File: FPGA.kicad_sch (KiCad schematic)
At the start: 15 parts, among them U3 XC7A100T-FTG256, U5 S25FL127S

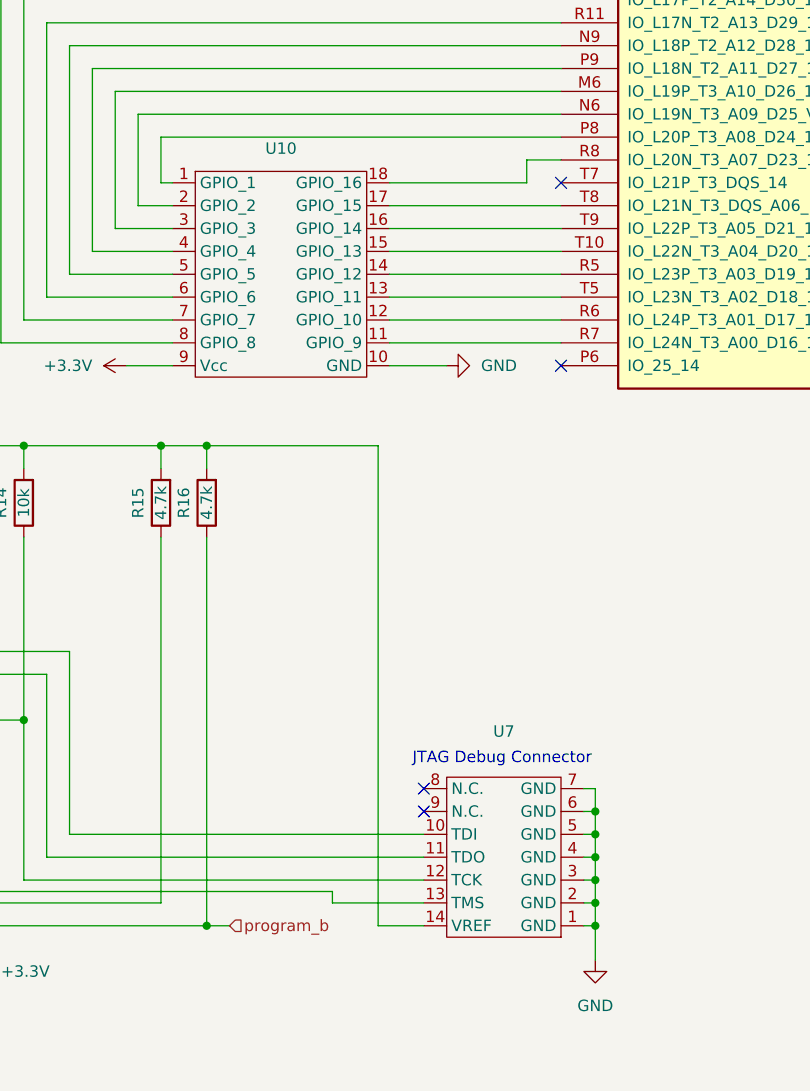
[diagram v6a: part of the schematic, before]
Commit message: Corrected FPGA Debug pin order
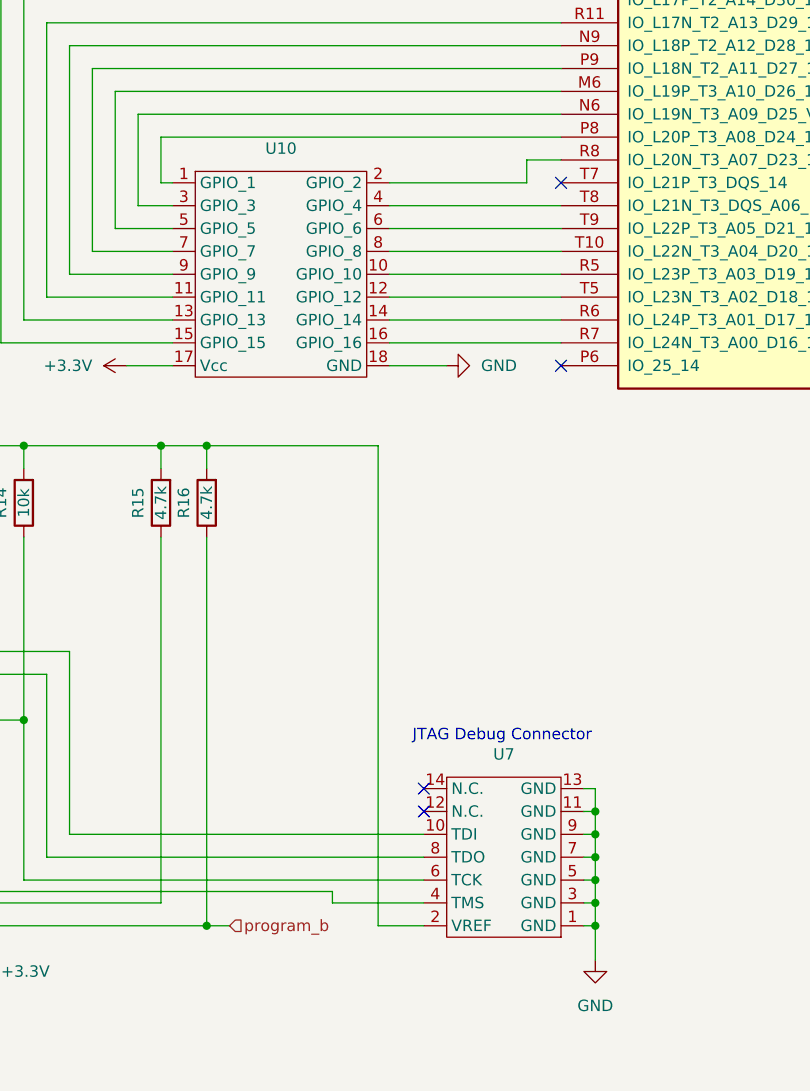
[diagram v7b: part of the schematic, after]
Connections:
- net +3.3V: now also U10.17 (Vcc), U7.2 (VREF); no longer U10.9 (Vcc), U7.14 (VREF)
- net GND: now also U10.18 (GND), U7.11 (GND), U7.13 (GND), U7.9 (GND); no longer U10.10 (GND), U7.2 (GND), U7.4 (GND), U7.6 (GND)
- net at R14.1, U3.L7 (TCK_0): now also U7.6 (TCK); no longer U7.12 (TCK)
- net at U3.M6 (IO_L19P_T3_A10_D26_14): now also U10.5 (GPIO_5); no longer U10.3 (GPIO_3)
- net at U3.N6 (IO_L19N_T3_A09_D25_VREF_14): now also U10.3 (GPIO_3); no longer U10.2 (GPIO_2)
- net at U3.N9 (IO_L18P_T2_A12_D28_14): now also U10.9 (GPIO_9); no longer U10.5 (GPIO_5)
- net at U3.P9 (IO_L18N_T2_A11_D27_14): now also U10.7 (GPIO_7); no longer U10.4 (GPIO_4)
- net at U3.R10 (IO_L17P_T2_A14_D30_14): now also U10.13 (GPIO_13); no longer U10.7 (GPIO_7)
- net at U3.R11 (IO_L17N_T2_A13_D29_14): now also U10.11 (GPIO_11); no longer U10.6 (GPIO_6)
- net at U3.R5 (IO_L23P_T3_A03_D19_14): now also U10.10 (GPIO_10); no longer U10.14 (GPIO_12)
- net at U3.R6 (IO_L24P_T3_A01_D17_14): now also U10.14 (GPIO_14); no longer U10.12 (GPIO_10)
- net at U3.R7 (IO_L24N_T3_A00_D16_14): now also U10.16 (GPIO_16); no longer U10.11 (GPIO_9)
- net at U3.R8 (IO_L20N_T3_A07_D23_14): now also U10.2 (GPIO_2); no longer U10.18 (GPIO_16)
- net at U3.T10 (IO_L22N_T3_A04_D20_14): now also U10.8 (GPIO_8); no longer U10.15 (GPIO_13)
- net at U3.T13 (IO_L16N_T2_A15_D31_14): now also U10.15 (GPIO_15); no longer U10.8 (GPIO_8)
- net at U3.T5 (IO_L23N_T3_A02_D18_14): now also U10.12 (GPIO_12); no longer U10.13 (GPIO_11)
- net at U3.T8 (IO_L21N_T3_DQS_A06_D22_14): now also U10.4 (GPIO_4); no longer U10.17 (GPIO_15)
- net at U3.T9 (IO_L22P_T3_A05_D21_14): now also U10.6 (GPIO_6); no longer U10.16 (GPIO_14)
- net at R13.1, U3.M7 (TMS_0): now also U7.4 (TMS); no longer U7.13 (TMS)
- net at U3.N8 (TDO_0): now also U7.8 (TDO); no longer U7.11 (TDO)
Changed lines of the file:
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@@
     (stroke (width 0) (type default))
   )
-  (text "JTAG Debug Connector" (at 167.64 218.44 0)
+  (text "JTAG Debug Connector" (at 167.64 215.9 0)
     (effects (font (size 1.27 1.27)) (justify left bottom))
   )
@@
     )
   )
+  (symbol (lib_id "GuitarZero:GPIO_Pins") (at 152.4 157.48 0) (unit 1)
+    (in_bom yes) (on_board yes) (dnp no) (fields_autoplaced)
+    (property "Reference" "U10" (at 153.035 149.86 0)
+      (effects (font (size 1.27 1.27)))
+    )
+    (property "Value" "~" (at 149.86 157.48 0)
+      (effects (font (size 1.27 1.27)))
+    )
+    (property "Footprint" "" (at 149.86 157.48 0)
+      (effects (font (size 1.27 1.27)) hide)
+    )
+    (property "Datasheet" "" (at 149.86 157.48 0)
+      (effects (font (size 1.27 1.27)) hide)
+    )
+    (pin "1")
+    (pin "10")
+    (pin "11")
+    (pin "12")
+    (pin "13")
+    (pin "14")
+    (pin "15")
+    (pin "16")
+    (pin "17")
+    (pin "18")
+    (pin "2")
+    (pin "3")
+    (pin "4")
+    (pin "5")
+    (pin "6")
+    (pin "7")
+    (pin "8")
+    (pin "9")
+    (instances
+      (project "GuitarZero"
+        (path "/fba50eda-8593-4456-af98-ff56fd418a76/7788bc9b-1e55-4835-b7d3-ea790efb8c61"
+          (reference "U10") (unit 1)
+        )
+      )
+    )
+  )
   (symbol (lib_id "power:+3.3V") (at 213.36 22.86 0) (unit 1)
     (in_bom yes) (on_board yes) (dnp no) (fields_autoplaced)
@@
     )
   )
-  (symbol (lib_id "GuitarZero:GPIO_Pins") (at 152.4 157.48 0) (unit 1)
-    (in_bom yes) (on_board yes) (dnp no) (fields_autoplaced)
-    (property "Reference" "U10" (at 153.035 149.86 0)
-      (effects (font (size 1.27 1.27)))
-    )
-    (property "Value" "~" (at 149.86 157.48 0)
-      (effects (font (size 1.27 1.27)))
-    )
-    (property "Footprint" "" (at 149.86 157.48 0)
-      (effects (font (size 1.27 1.27)) hide)
-    )
-    (property "Datasheet" "" (at 149.86 157.48 0)
-      (effects (font (size 1.27 1.27)) hide)
-    )
-    (pin "1")
-    (pin "10")
-    (pin "11")
-    (pin "12")
-    (pin "13")
-    (pin "14")
-    (pin "15")
-    (pin "16")
-    (pin "17")
-    (pin "18")
-    (pin "2")
-    (pin "3")
-    (pin "4")
-    (pin "5")
-    (pin "6")
-    (pin "7")
-    (pin "8")
-    (pin "9")
-    (instances
-      (project "GuitarZero"
-        (path "/fba50eda-8593-4456-af98-ff56fd418a76/7788bc9b-1e55-4835-b7d3-ea790efb8c61"
-          (reference "U10") (unit 1)
-        )
-      )
-    )
-  )
   (symbol (lib_id "power:+3.3V") (at 91.44 181.61 0) (unit 1)
     (in_bom yes) (on_board yes) (dnp no) (fields_autoplaced)
@@
     )
   )
+  (symbol (lib_id "power:PWR_FLAG") (at 234.95 217.17 0) (unit 1)
+    (in_bom yes) (on_board yes) (dnp no) (fields_autoplaced)
+    (property "Reference" "#FLG02" (at 234.95 215.265 0)
+      (effects (font (size 1.27 1.27)) hide)
+    )
+    (property "Value" "PWR_FLAG" (at 234.95 212.09 0)
+      (effects (font (size 1.27 1.27)))
+    )
+    (property "Footprint" "" (at 234.95 217.17 0)
+      (effects (font (size 1.27 1.27)) hide)
+    )
+    (property "Datasheet" "~" (at 234.95 217.17 0)
+      (effects (font (size 1.27 1.27)) hide)
+    )
+    (pin "1")
+    (instances
+      (project "GuitarZero"
+        (path "/fba50eda-8593-4456-af98-ff56fd418a76/7788bc9b-1e55-4835-b7d3-ea790efb8c61"
+          (reference "#FLG02") (unit 1)
+        )
+      )
+    )
+  )
+  (symbol (lib_id "Device:C") (at 48.26 58.42 0) (unit 1)
+    (in_bom yes) (on_board yes) (dnp no)
+    (property "Reference" "C52" (at 49.53 55.88 0)
+      (effects (font (size 1.27 1.27)) (justify left))
+    )
+    (property "Value" "100n" (at 49.53 60.96 0)
+      (effects (font (size 1.27 1.27)) (justify left))
+    )
+    (property "Footprint" "" (at 49.2252 62.23 0)
+      (effects (font (size 1.27 1.27)) hide)
+    )
+    (property "Datasheet" "~" (at 48.26 58.42 0)
+      (effects (font (size 1.27 1.27)) hide)
+    )
+    (pin "1")
+    (pin "2")
+    (instances
+      (project "GuitarZero"
+        (path "/fba50eda-8593-4456-af98-ff56fd418a76/7788bc9b-1e55-4835-b7d3-ea790efb8c61"
+          (reference "C52") (unit 1)
+        )
+      )
+    )
+  )
   (symbol (lib_id "GuitarZero:FPGA_JTAG_Connector") (at 180.34 232.41 180) (unit 1)
-    (in_bom yes) (on_board yes) (dnp no)
-    (property "Reference" "U7" (at 177.8 214.63 0)
+    (in_bom yes) (on_board yes) (dnp no) (fields_autoplaced)
+    (property "Reference" "U7" (at 177.8 217.17 0)
       (effects (font (size 1.27 1.27)))
     )
@@
         )
       )
-    )
-  )
-  (symbol (lib_id "power:PWR_FLAG") (at 234.95 217.17 0) (unit 1)
-    (in_bom yes) (on_board yes) (dnp no) (fields_autoplaced)
-    (property "Reference" "#FLG02" (at 234.95 215.265 0)
-      (effects (font (size 1.27 1.27)) hide)
-    )
-    (property "Value" "PWR_FLAG" (at 234.95 212.09 0)
-      (effects (font (size 1.27 1.27)))
-    )
-    (property "Footprint" "" (at 234.95 217.17 0)
-      (effects (font (size 1.27 1.27)) hide)
-    )
-    (property "Datasheet" "~" (at 234.95 217.17 0)
-      (effects (font (size 1.27 1.27)) hide)
-    )
-    (pin "1")
-    (instances
-      (project "GuitarZero"
-        (path "/fba50eda-8593-4456-af98-ff56fd418a76/7788bc9b-1e55-4835-b7d3-ea790efb8c61"
-          (reference "#FLG02") (unit 1)
-        )
-      )
-    )
-  )
-  (symbol (lib_id "Device:C") (at 48.26 58.42 0) (unit 1)
-    (in_bom yes) (on_board yes) (dnp no)
-    (property "Reference" "C52" (at 49.53 55.88 0)
-      (effects (font (size 1.27 1.27)) (justify left))
-    )
-    (property "Value" "100n" (at 49.53 60.96 0)
-      (effects (font (size 1.27 1.27)) (justify left))
-    )
-    (property "Footprint" "" (at 49.2252 62.23 0)
-      (effects (font (size 1.27 1.27)) hide)
-    )
-    (property "Datasheet" "~" (at 48.26 58.42 0)
-      (effects (font (size 1.27 1.27)) hide)
-    )
-    (pin "1")
-    (pin "2")
-    (instances
-      (project "GuitarZero"
-        (path "/fba50eda-8593-4456-af98-ff56fd418a76/7788bc9b-1e55-4835-b7d3-ea790efb8c61"
-          (reference "C52") (unit 1)
-        )
-      )

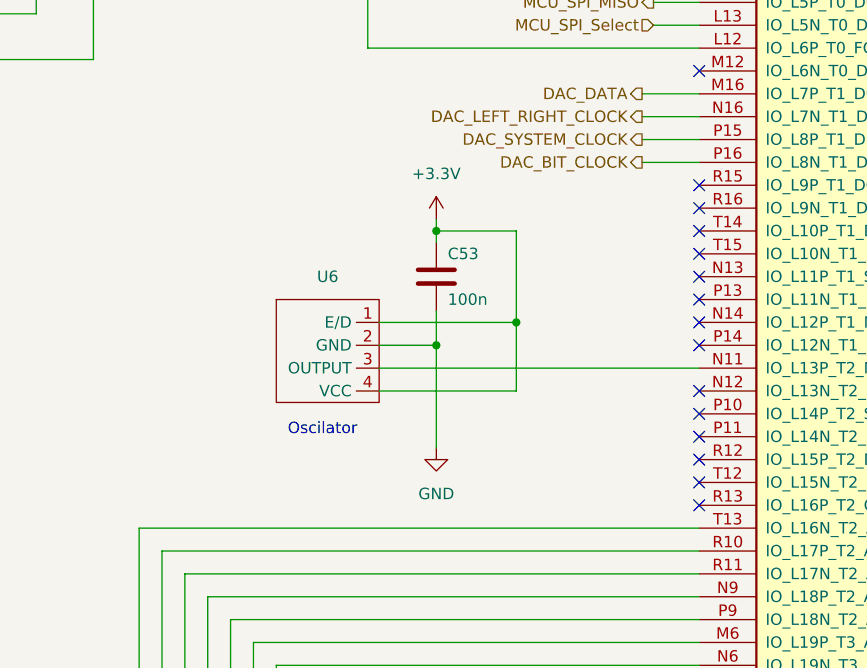
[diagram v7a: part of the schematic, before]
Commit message: Added FPGA debug led
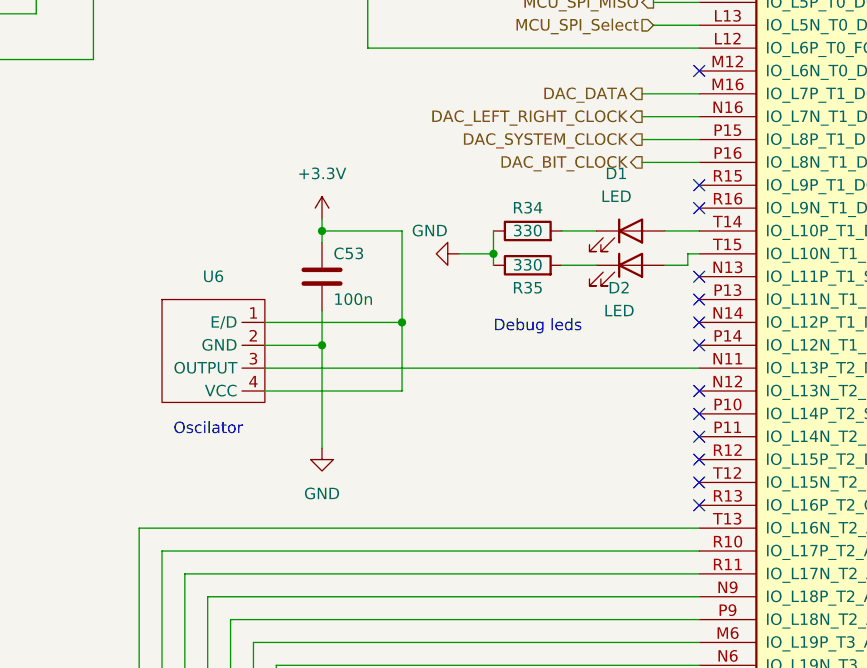
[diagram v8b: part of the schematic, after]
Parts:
- added D1, D2: LED, symbol Device:LED
- added R34, R35: 330, symbol Device:R
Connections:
- net GND: now also R34.1, R35.1
- net at U3.T14 (IO_L10P_T1_D14_14): now also D1.2 (A)
- net at U3.T15 (IO_L10N_T1_D15_14): now also D2.2 (A)
- new net: D2.1 (K), R35.2
- new net: D1.1 (K), R34.2
- no-connect marks 143 -> 141
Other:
- note added: "Debug leds"
- moved on the sheet: C53, U6
